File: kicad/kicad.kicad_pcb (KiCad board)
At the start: 2 copper layers, 31.8 x 37.3 mm, 101 parts, among them J201 USB_C_Receptacle_USB2.0_16P, J301 BATTERY_CONN, Q301 2N7002, Q401 Si1308EDL, Q701 2N7002, SW101 PWR_SWITCH, SW601 BT1, SW602 BT3, SW603 BT2, SW604 BT4, U301 BQ25185, U302 TPS7A20, U501 DA7280, U701 MLPF-WB55-01E3, U702 STM32WB55RGVx, Y701 32M

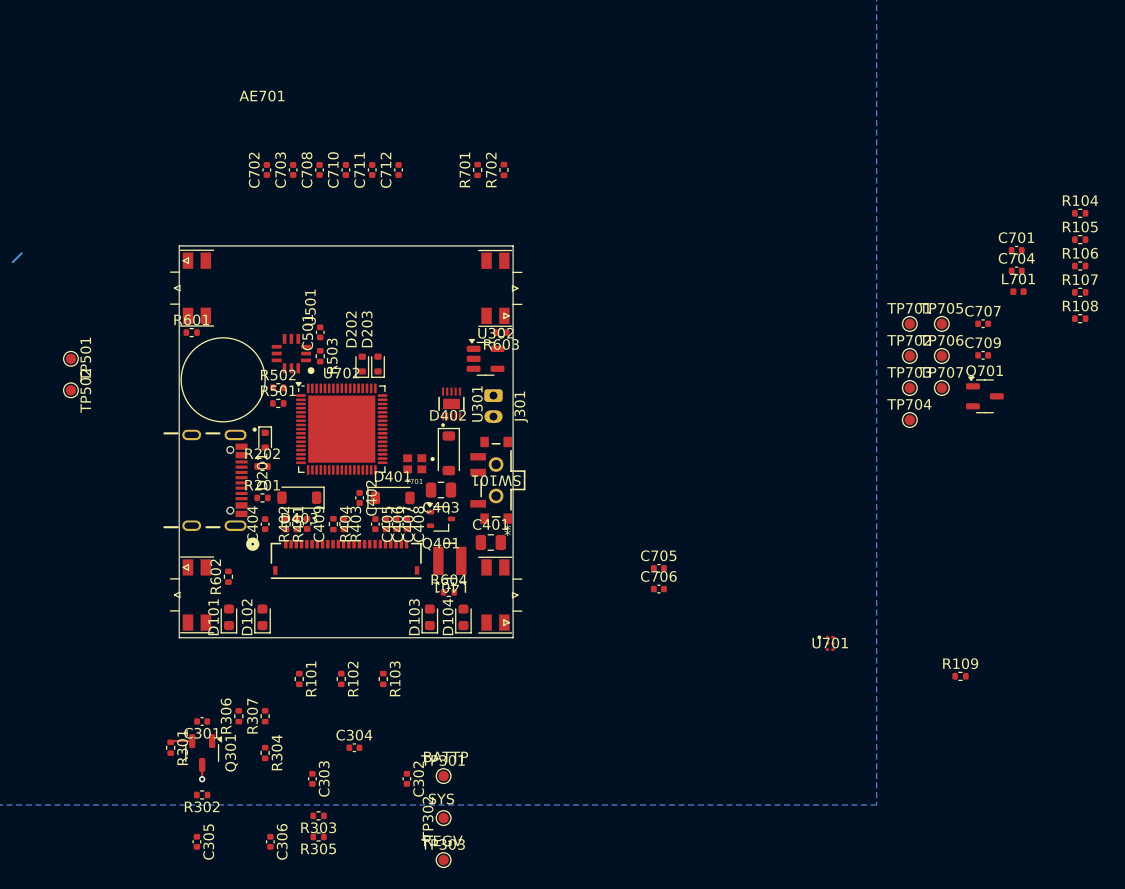
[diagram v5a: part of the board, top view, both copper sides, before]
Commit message: Finish PCB component placement
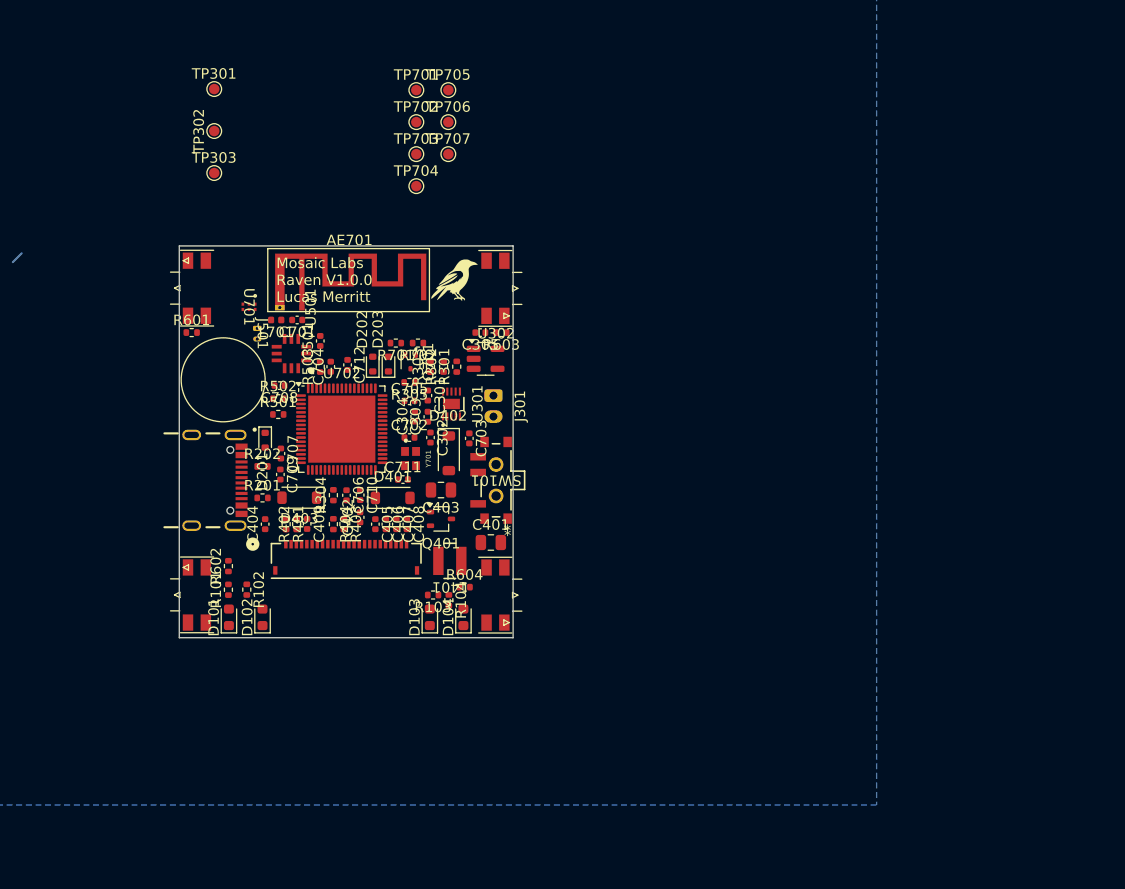
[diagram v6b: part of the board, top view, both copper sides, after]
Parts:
- removed the C301 at (128.8, 139.1)
- removed Q301: 2N7002, Package_TO_SOT_SMD:SOT-23-3
- removed the R101 at (138.0, 135.0)
- removed the R102 at (142.0, 135.0)
- removed the R103 at (146.0, 135.0)
- removed the R104 at (212.4, 90.6)
- removed R109: 0, Resistor_SMD:R_0402_1005Metric
- removed the R301 at (125.8, 141.6)
- removed the R304 at (134.8, 142.1)
- removed TP501: OUTP_PAD, TestPoint:TestPoint_Pad_D1.0mm
- removed TP502: OUTN_PAD, TestPoint:TestPoint_Pad_D1.0mm
- added G***: LOGO, LOGO, F.Cu at (153.0, 97.0)
- added J501: MOTOR_CONN, Raven:CUSTOM_MOTOR_CONN, F.Cu at (134.0, 102.1)
- AE701: footprint Raven:AN3359_ANT -> RF_Antenna:Texas_SWRA117D_2.4GHz_Right
- Q701: value 2N7002 -> DMG1012T; footprint Package_TO_SOT_SMD:SOT-23-3 -> Package_TO_SOT_SMD:SOT-523
- moved AE701 110.8 mm to (138.2, 99.6)
- moved R101 87.7 mm to (131.2, 126.5), turned to 90 degrees
- moved R102 85.2 mm to (133.0, 126.5), turned to -90 degrees
- moved L701 70.8 mm to (135.8, 100.8), turned to 180 degrees
- moved TP301 69.0 mm to (129.9, 78.8)
- moved TP302 69.0 mm to (129.9, 82.8)
- moved TP303 69.0 mm to (129.9, 86.8)
- moved C701 68.9 mm to (137.8, 100.8), turned to 180 degrees
- moved R103 68.1 mm to (150.8, 127.0), turned to 180 degrees
- moved C707 68.0 mm to (136.2, 113.5), turned to -90 degrees
- moved C709 67.9 mm to (136.2, 115.5), turned to -90 degrees
- moved C704 66.0 mm to (141.0, 105.2), turned to 90 degrees
- moved R104 65.9 mm to (152.2, 127.5), turned to -90 degrees
- moved U701 64.0 mm to (133.2, 99.5), turned to -90 degrees
- moved Q701 54.8 mm to (148.6, 104.8), turned to -90 degrees
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- renumbered C302 to C301, C303 to C302, C304 to C303, C305 to C304, C306 to C305, R105 to R101, R106 to R102, R107 to R103, R108 to R104, R302 to R301, R303 to R302, R305 to R303, R306 to R304, R307 to R305
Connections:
- C301 pad 1: /Battery Management/CHRG -> VBUS
- C401 pad 1: /E-Paper Display/PWR -> +3.3V
- C501 pad 1: /Haptics/PWR -> +3.3V
- C702 pad 1: /Microcontroller/SMPS -> +3.3V
- C703 pad 1: /Microcontroller/SMPS -> +3.3V
- C704 pad 1: /Microcontroller/SMPS -> +3.3V
- C705 pad 1: /Microcontroller/SMPS -> +3.3V
- C706 pad 1: /Microcontroller/SMPS -> +3.3V
- C707 pad 1: /Microcontroller/SMPS -> +3.3V
- C708 pad 1: /Microcontroller/SMPS -> +3.3V
- C709 pad 1: /Microcontroller/SMPS -> +3.3V
- C710 pad 1: /Microcontroller/SMPS -> +3.3V
- C711 pad 1: /Microcontroller/SMPS -> +3.3V
- C712 pad 2: /Microcontroller/SMPS -> +3.3V
- EPD_FPC401 pad 15: /E-Paper Display/PWR -> +3.3V
- EPD_FPC401 pad 16: /E-Paper Display/PWR -> +3.3V
- L401 pad 2: /E-Paper Display/PWR -> +3.3V
- Q701 pad 1: Net-(Q701-D) -> /Input/BT1
- Q701 pad 2: /Input/BT1 -> GND
- Q701 pad 3: GND -> Net-(Q701-D)
- R304 pad 1: /Battery Management/CHRG -> /Battery Management/SYS_T
- R305 pad 1: /Battery Management/CHRG -> /Battery Management/SYS_T
- R403 pad 1: /E-Paper Display/PWR -> +3.3V
- R404 pad 1: /E-Paper Display/PWR -> +3.3V
- R501 pad 1: /Haptics/PWR -> +3.3V
- R502 pad 1: /Haptics/PWR -> +3.3V
- R503 pad 1: /Haptics/PWR -> +3.3V
- R601 pad 1: /Input/PULL_UP -> +3.3V
- R602 pad 1: /Input/PULL_UP -> +3.3V
- R603 pad 1: /Input/PULL_UP -> +3.3V
- R604 pad 1: /Input/PULL_UP -> +3.3V
- R702 pad 1: /Microcontroller/SMPS -> +3.3V
- TP707 pad 1: /Microcontroller/SMPS -> +3.3V
- U301 pad 10: /Battery Management/CHRG -> VBUS
- U501 pad 4: /Haptics/PWR -> +3.3V
- U501 pad 9: /Haptics/PWR -> +3.3V
- U702 pad 1: /Microcontroller/SMPS -> +3.3V
- U702 pad 13: /Microcontroller/SMPS -> +3.3V
- U702 pad 14: /Microcontroller/SMPS -> +3.3V
- U702 pad 23: /Battery Management/MR_CTRL -> /Microcontroller/BAT_MR
- U702 pad 30: /Microcontroller/SMPS -> +3.3V
- U702 pad 33: /Microcontroller/SMPS -> +3.3V
- U702 pad 41: /Microcontroller/SMPS -> +3.3V
- U702 pad 43: /Microcontroller/SMPS -> +3.3V
- U702 pad 44: /Microcontroller/SMPS -> +3.3V
- U702 pad 45: /Microcontroller/SMPS -> +3.3V
- U702 pad 55: /Microcontroller/SMPS -> +3.3V
- U702 pad 68: /Microcontroller/SMPS -> +3.3V
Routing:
- net /Battery Management/MR_CTRL: track 1.77 -> 0.00 mm
- net GND: track 6.08 -> 4.72 mm, vias 1 -> 0
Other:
- board text added: "Mosaic Labs Raven V1.0.0 Lucas Merritt"
- board text removed: "BATTP"
- board text removed: "REGV"
- board text removed: "SYS"

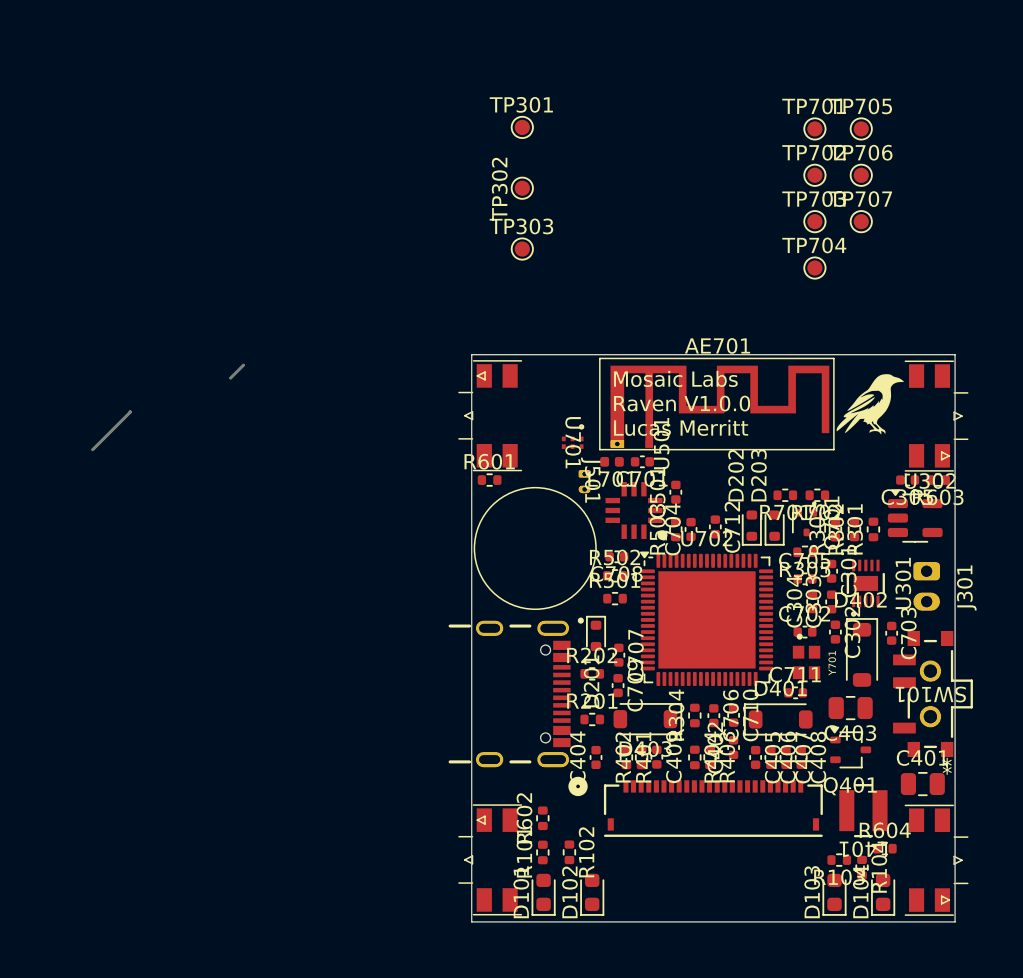
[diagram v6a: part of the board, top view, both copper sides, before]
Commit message: PCB Trace progress
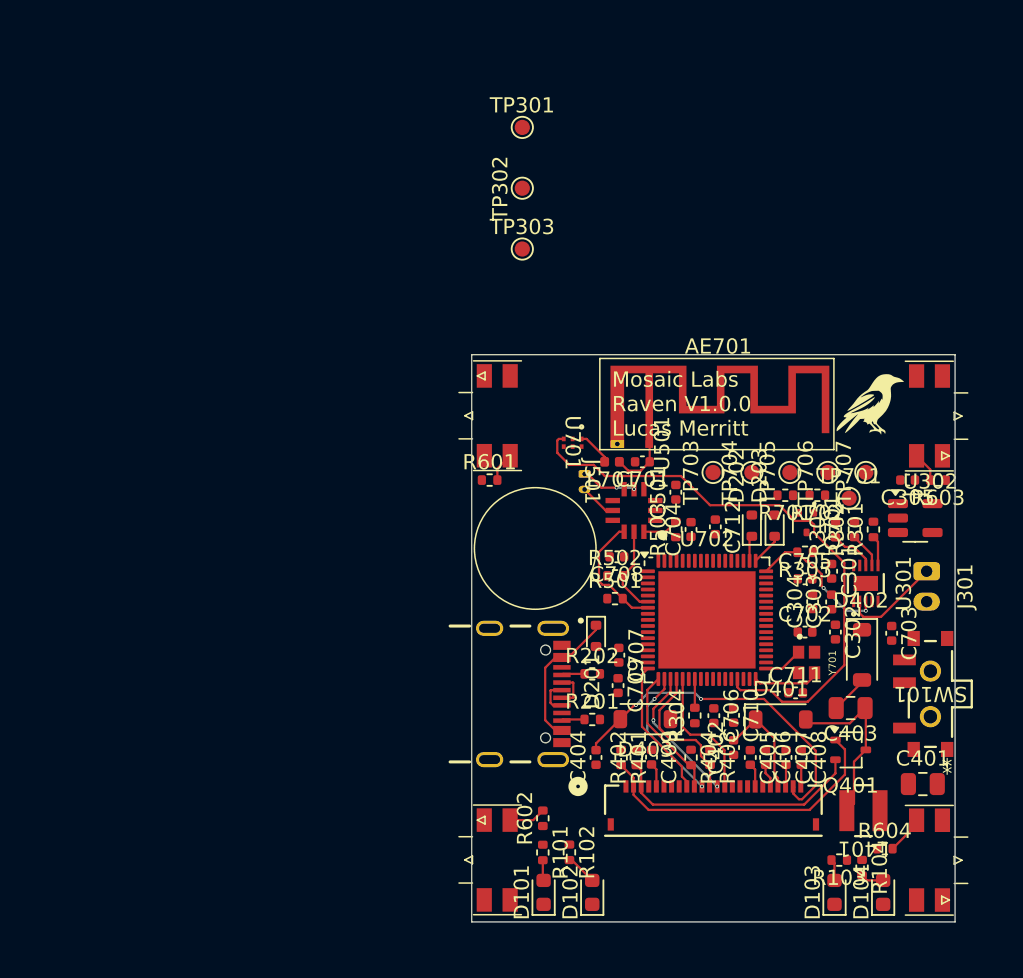
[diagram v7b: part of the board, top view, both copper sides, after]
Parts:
- removed TP702: NRST_PAD, TestPoint:TestPoint_Pad_D1.0mm
- moved TP701 24.4 mm to (151.4, 103.2)
- moved TP705 23.1 mm to (147.5, 101.5), turned to 90 degrees
- moved TP706 19.7 mm to (150.0, 101.5), turned to 90 degrees
- moved TP703 17.8 mm to (142.4, 101.5), turned to 90 degrees
- moved TP707 16.5 mm to (152.5, 101.5), turned to 90 degrees
- moved TP704 14.1 mm to (145.0, 101.5), turned to 90 degrees
- moved C405 0.35 mm to (144.9, 120.2)
- moved C406 0.35 mm to (145.9, 120.2)
- moved C409 0.35 mm to (138.4, 120.2)
- moved R401 0.35 mm to (136.4, 120.2)
- moved R402 0.35 mm to (137.4, 120.2)
- moved R404 0.25 mm to (141.0, 120.2)
- turned R101 to -90 degrees
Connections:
- R101 pad 1: +3V3 -> +3.3V
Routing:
- net Net-(U701-IN): track 0.00 -> 39.2 mm
- net /E-Paper Display/PREVGL: track 0.00 -> 22.7 mm, vias 0 -> 2
- net /E-Paper Display/GDR: track 0.00 -> 20.1 mm
- net /E-Paper Display/RESE: track 0.00 -> 17.1 mm
- net Net-(D401-A): track 0.00 -> 11.7 mm
- net /E-Paper Display/CS_N: track 0.00 -> 9.86 mm
- net /Battery Management/STAT2: track 0.00 -> 9.75 mm, vias 0 -> 2
- net VBUS: track 0.00 -> 9.51 mm
- net /E-Paper Display/SCK: track 0.00 -> 9.27 mm, vias 0 -> 2
- net /E-Paper Display/BUSY: track 0.00 -> 9.14 mm
- net /E-Paper Display/DC: track 0.00 -> 9.02 mm, vias 0 -> 2
- net /E-Paper Display/MOSI: track 0.00 -> 8.93 mm
- net /E-Paper Display/RES_N: track 0.00 -> 8.73 mm
- net /Haptics/SDA: track 0.00 -> 8.07 mm
- net /E-Paper Display/PREVGH: track 0.00 -> 7.03 mm
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- added copper zone on In2.Cu, net +3.3V
- added copper zone on In1.Cu, net GND
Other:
- copper layers 2 -> 4

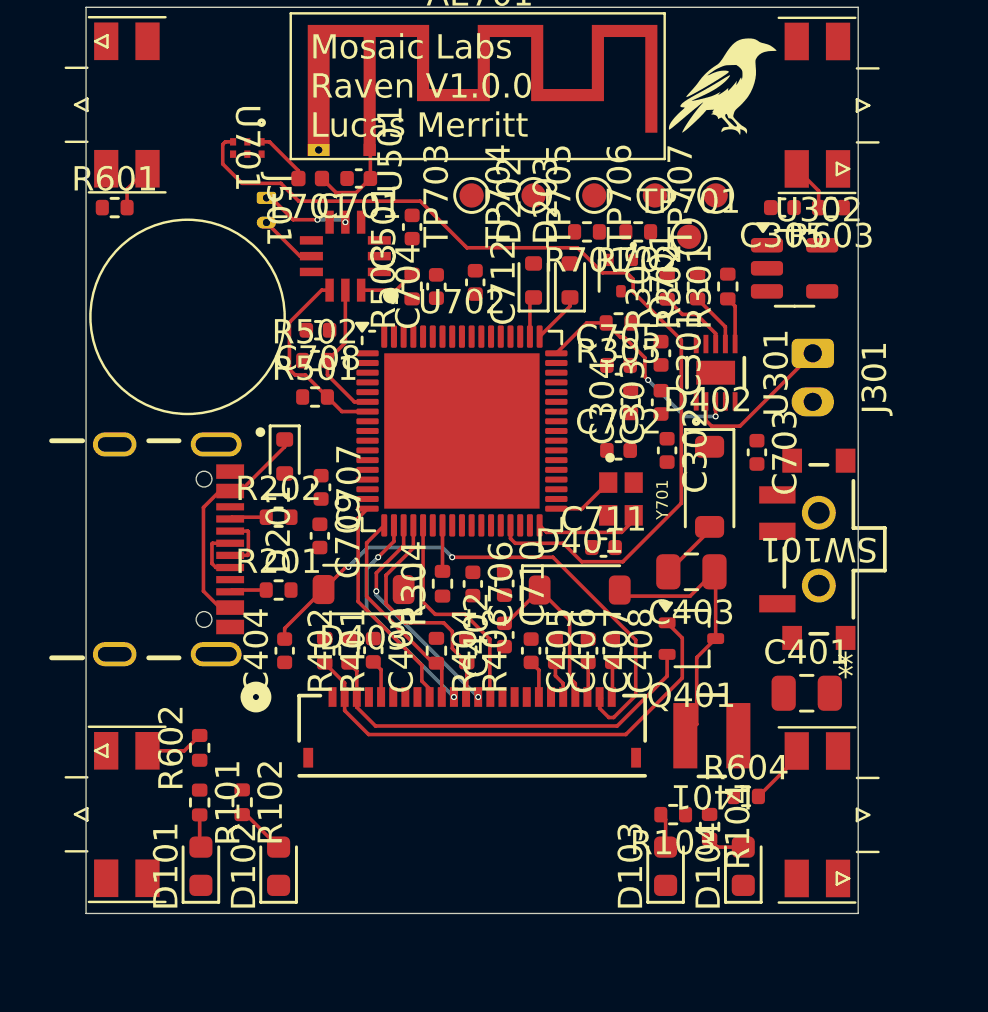
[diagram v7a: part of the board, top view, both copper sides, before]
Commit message: Minor schematic fixes and PCB trace progress
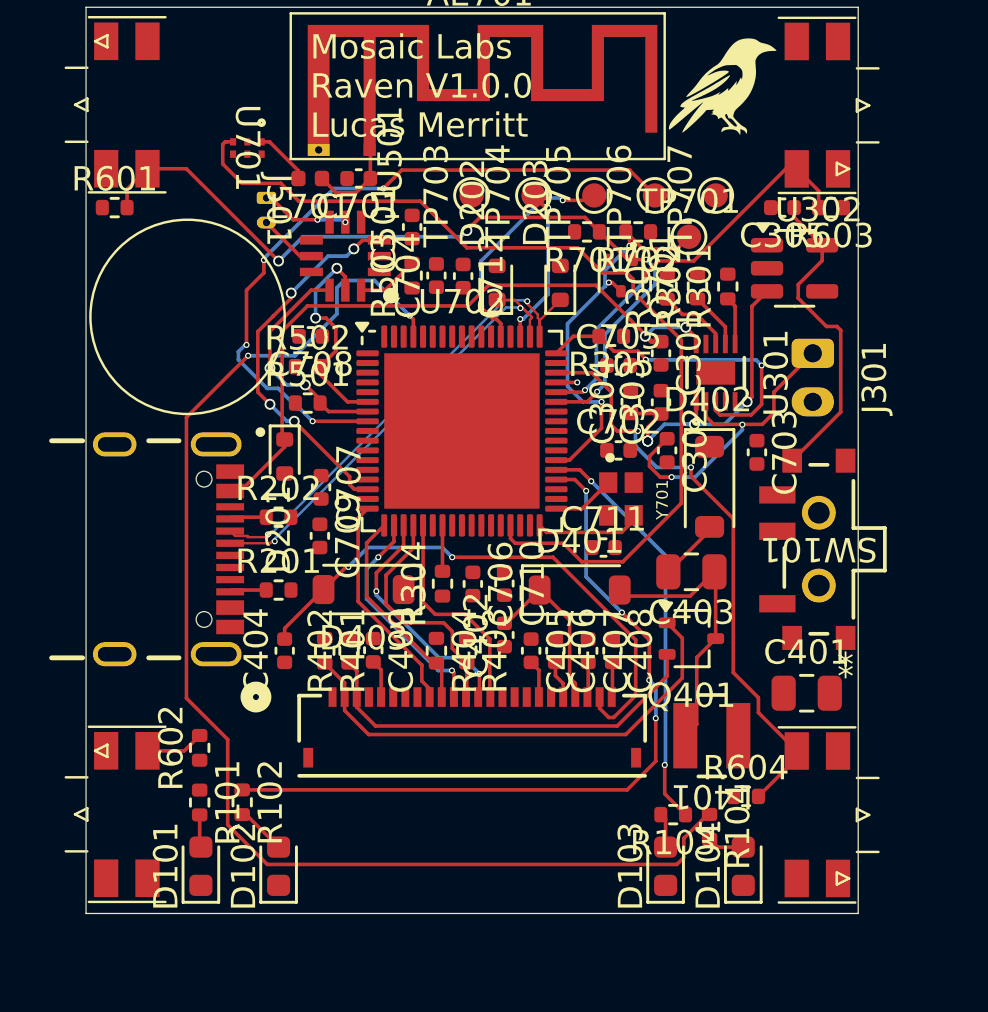
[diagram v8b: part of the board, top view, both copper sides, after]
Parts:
- moved D202 1.50 mm to (143.5, 105.1)
- moved R305 0.63 mm to (148.2, 107.3)
- moved C712 0.56 mm to (142.1, 104.8)
- moved C704 0.45 mm to (141.0, 104.8)
- moved R503 0.45 mm to (140.0, 104.8)
- moved D203 0.41 mm to (146.1, 105.1)
- moved C708 0.39 mm to (135.8, 107.3)
- moved R501 0.39 mm to (135.7, 110.0)
- moved R502 0.39 mm to (135.7, 108.5)
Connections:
- net /Microcontroller/DM renamed /Microcontroller/D-
- net /Microcontroller/DP renamed /Microcontroller/D+
- R304 pad 1: /Battery Management/SYS_T -> +3.3V
- R305 pad 1: /Battery Management/SYS_T -> +3.3V
- U702 pad 23: /Microcontroller/BAT_MR -> unconnected-(U702-PA8-Pad23)
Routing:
- net /Microcontroller/LED_F2: track 0.00 -> 53.0 mm, vias 0 -> 2
- net /Input/BT1: track 1.95 -> 34.0 mm, vias 0 -> 4
- net /Microcontroller/LED_BATT: track 0.00 -> 31.3 mm, vias 0 -> 4
- net /Microcontroller/NRST: track 0.00 -> 29.0 mm, vias 0 -> 4
- net /Input/BT4: track 2.53 -> 24.5 mm, vias 0 -> 2
- net VBUS: track 9.51 -> 28.6 mm, vias 0 -> 2
- net /Microcontroller/LED_F1: track 0.00 -> 17.0 mm, vias 0 -> 2
- net Net-(Q701-D): track 0.00 -> 16.6 mm, vias 0 -> 3
- net /Haptics/GPI_0: track 0.00 -> 15.5 mm, vias 0 -> 4
- net /Input/BT2: track 1.97 -> 17.0 mm, vias 0 -> 2
- net /Microcontroller/D+: track 4.06 -> 19.1 mm, vias 0 -> 2
- net /Microcontroller/D-: track 4.60 -> 19.4 mm, vias 0 -> 2
- net /Battery Management/SYS_T: track 0.00 -> 13.5 mm, vias 0 -> 4
- net REGV: track 0.00 -> 13.1 mm
- net /Microcontroller/SWCLK: track 0.00 -> 9.39 mm, vias 0 -> 2
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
